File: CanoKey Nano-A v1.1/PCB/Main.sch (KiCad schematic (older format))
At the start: 31 parts, among them J1 USB_A_PCB, U1 FM11NC08S, U2 USBLC6-2SC6, U3 STM32L432KCUx, U4 AP7331-33SNG-7

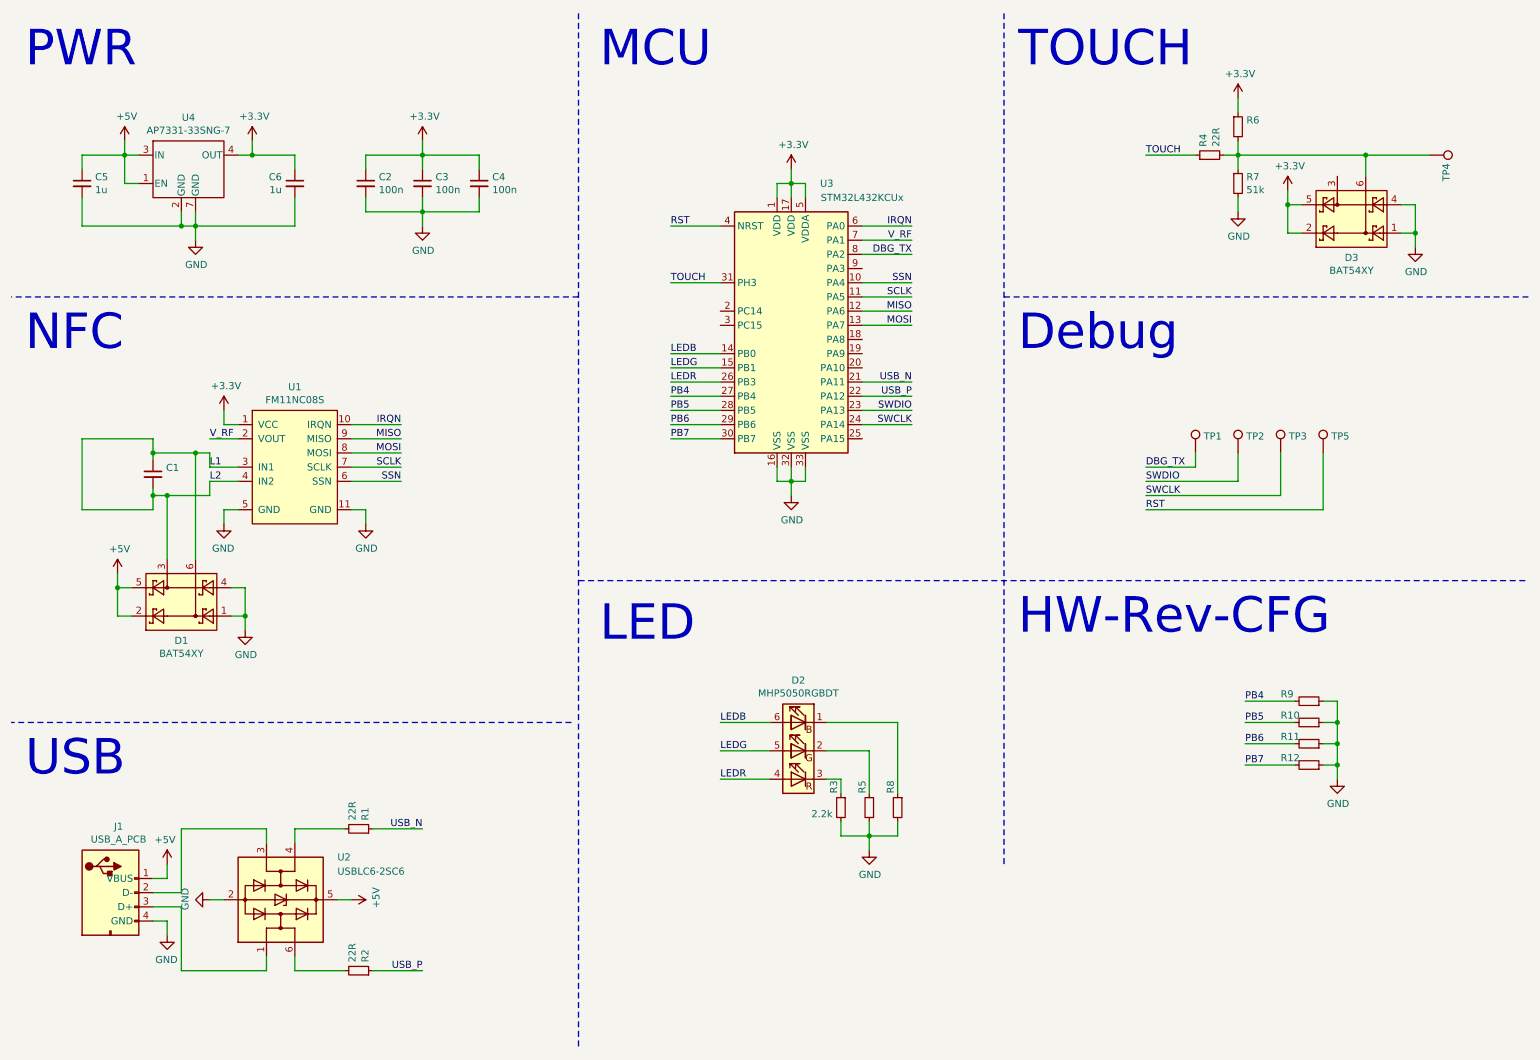
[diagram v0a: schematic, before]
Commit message: add sch to nano v1.1
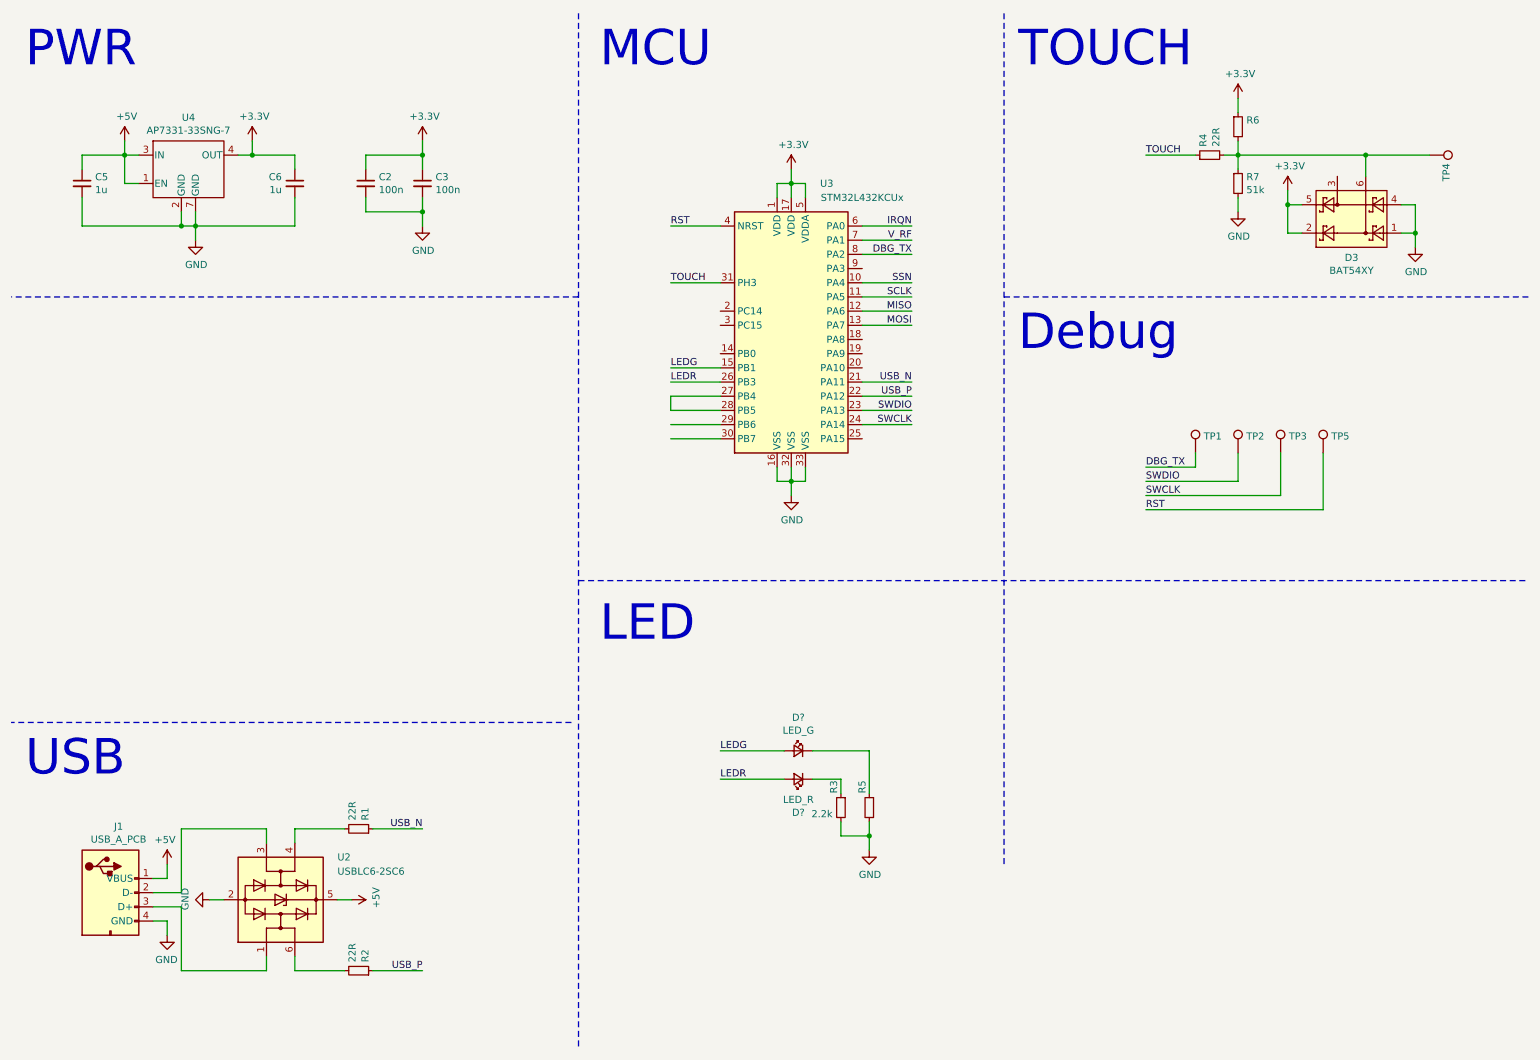
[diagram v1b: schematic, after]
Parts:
- removed C1: ~, Capacitor_SMD:C_0603_1608Metric, symbol Device:C_Small
- removed C4: 100n, Capacitor_SMD:C_0603_1608Metric, symbol Device:C_Small
- removed D1: BAT54XY, Package_TO_SOT_SMD:SOT-363_SC-70-6, symbol MAS_Diode:BAT54XY
- removed D2: MHP5050RGBDT, LED_SMD:LED_RGB_5050-6, symbol MAS_Diode:MHP5050RGBDT
- removed R10, R11, R12, R9: ~, Resistor_SMD:R_0603_1608Metric, symbol Device:R_Small
- removed R8: 2.2k, Resistor_SMD:R_0603_1608Metric, symbol Device:R_Small
- removed U1: FM11NC08S, Package_DFN_QFN:DFN-10-1EP_3x3mm_P0.5mm_EP1.55x2.48mm, symbol MAS_IC_Interface:FM11NC08S
- added D?: LED_G, Diode_SMD:D_0805_2012Metric, symbol Device:LED_Small
- added D?: LED_R, Diode_SMD:D_0805_2012Metric, symbol Device:LED_Small
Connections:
- net PB5 is gone; now on an unnamed net: U3.28 (PB5)
- net LEDG: now also D?.2 (A)
- net LEDR: now also D?.2 (A)
- net at R5.1: now also D?.1 (K)
- net at R3.1: now also D?.1 (K)
- net LEDB: no longer names the net of U3.14 (PB0)
- net PB4: no longer names the net of U3.27 (PB4)
- net PB6: no longer names the net of U3.29 (PB6)
- net PB7: no longer names the net of U3.30 (PB7)
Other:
- note removed: "HW-Rev-CFG"
- note removed: "NFC"
